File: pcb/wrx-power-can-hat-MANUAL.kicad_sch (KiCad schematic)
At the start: 65 parts, among them J1 ISO_A, J2 Pi_GPIO, J3 OBD-II, J4 CAN_Term, J5 ISP, J6 FAN, J7 Audio, Q1 IRLB8721PBF, Q2 2N7002, Q3 2N7002, U1 TPS54560BDDA, U2 LTV-817S, U3 attiny85, U4 MCP2515, U5 SN65HVD230, U6 AMS1117-3.3, Y1 16MHz, Y2 16Mhz Crystal

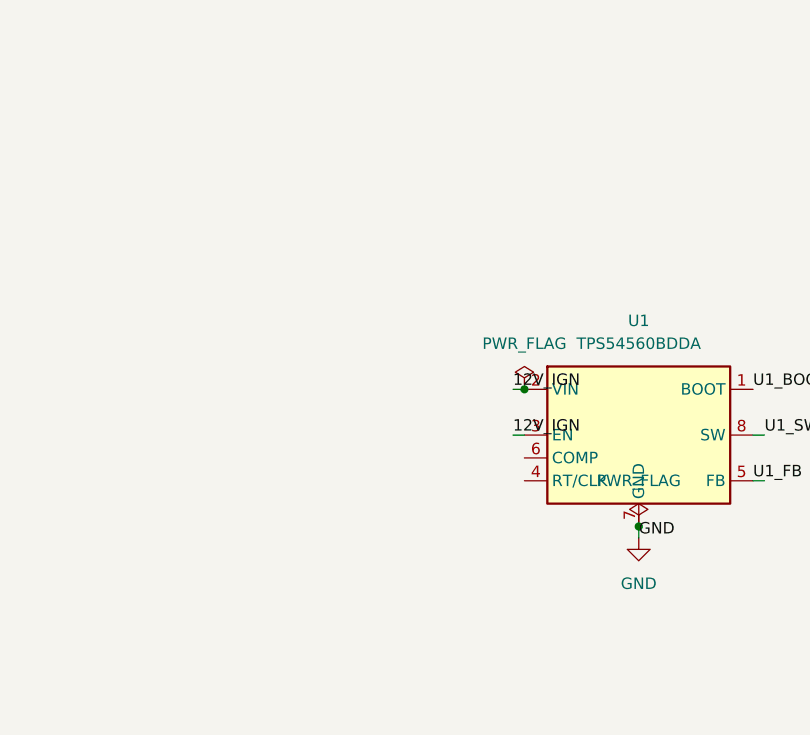
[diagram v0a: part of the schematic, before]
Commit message: Add TPS54560 compensation network - achieve 0 ERC errors
- Added R_RT timing resistor for U1 Pin 4 (RT/CLK)
- Added R_COMP and C_COMP series RC network for U1 Pin 6 (COMP)
- Used labels U1_RT, U1_COMP, COMP_RC for clean connections
- ERC reduced from 2 errors to 0 errors (47 warnings remaining)
- All warnings are expected (same_local_global_label, dangling globals, etc.)

Co-Authored-By: Claude Opus 4.5 <noreply@anthropic.com>
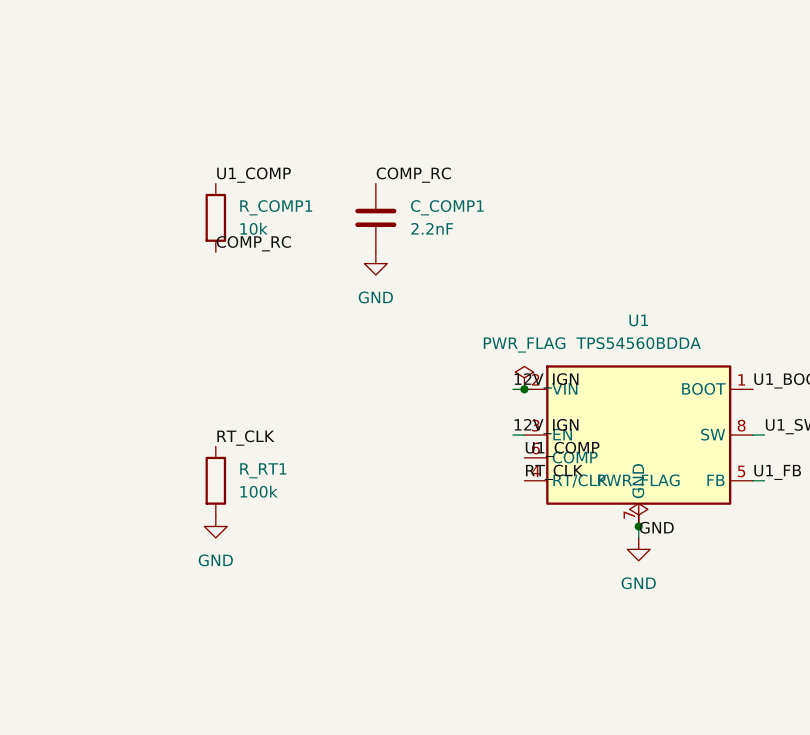
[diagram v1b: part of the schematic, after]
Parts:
- added C_COMP1: 2.2nF, symbol Device:C
- added R_COMP1: 10k, symbol Device:R
- added R_RT1: 100k, symbol Device:R
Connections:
- net GND: now also C_COMP1.2, R_RT1.2
- net RT_CLK: now reaches U1.4 (RT/CLK)
- net RT_CLK: now also R_RT1.1
- net U1_COMP: now reaches U1.6 (COMP)
- net U1_COMP: now also R_COMP1.1
- new net COMP_RC: C_COMP1.1, R_COMP1.2

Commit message: Add schematic improvements for reliability
Changes:
- R4/R5: Changed to 1% tolerance (10k 1%, 51k 1%) for accurate Vout
- R20: Changed from 1k to 470Ω for faster gate drive switching
- C20: Added 22µF input bulk capacitor parallel to C10
- L2/L3: Added ferrite beads for CAN bus EMI filtering
  - Signal flow: U5 → CANH_U5/CANL_U5 → L2/L3 → CANH/CANL

ERC: 0 errors, 50 warnings (all informational)

Co-Authored-By: Claude Opus 4.5 <noreply@anthropic.com>
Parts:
- added C20: 22uF, symbol Device:C
- added L2, L3: Ferrite, symbol Device:L
- R20: value 1k -> 470
- R4: value 10k -> 10k 1%
- R5: value 51k -> 51k 1%
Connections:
- net 12V_IGN: now also C20.1
- net CANH: now also L2.2; no longer U5.7 (CANH)
- net CANL: now also L3.2; no longer U5.6 (CANL)
- net GND: now also C20.2
- new net CANH_U5: L2.1, U5.7 (CANH)
- new net CANL_U5: L3.1, U5.6 (CANL)
